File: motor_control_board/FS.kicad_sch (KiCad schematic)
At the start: 18 parts

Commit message: Minor schematic edits
Annotated schematic, selected mosfet and diodes, addressed comments
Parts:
- removed C?: 100n, symbol canhw:C
- removed JP?: Jumper, symbol canhw:SolderJumper_2_Open
- removed R?: 10k, symbol canhw:R_US
- C? (x2): value 15p -> 26p
- X?: value 16MHz -> 12MHz
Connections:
- net MCLR_FS: now also C?.1
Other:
- note added: "DNM when programming"
- note added: "Debug LEDs"
- note added: "Series resistor if necessary"
- moved on the sheet: C?

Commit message: Added second encoder connection, minor edits
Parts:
- added R14, R17: 10k, symbol Device:R_US
- C7: renamed from C?; value 100n -> 10u
- gave numbers to parts that had none: 14
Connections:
- net +5V: now also R14.1
- net FS_MCU: now also R17.1
- net GND: now also R17.2
- net MCLR_FS: now also R14.2
- net ENC2: now reaches U5.18 (RC7)
- net ENC renamed ENC1
- no-connect marks 9 -> 8
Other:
- note added: "DNP until flight"
- note removed: "DNM when programming"

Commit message: assigned footprints
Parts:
- C10, C11, C7, C8, C9: footprint (none) -> Capacitor_SMD:C_0805_2012Metric_Pad1.18x1.45mm_HandSolder
- D7, D8: footprint (none) -> LED_SMD:LED_1206_3216Metric_Pad1.42x1.75mm_HandSolder
- R11, R12, R13, R14, R15, R16, R17: footprint (none) -> Resistor_SMD:R_0805_2012Metric_Pad1.20x1.40mm_HandSolder
- U4: footprint (none) -> Package_SO:SOIC-8_3.9x4.9mm_P1.27mm
- U5: footprint (none) -> Package_SO:SSOP-28_5.3x10.2mm_P0.65mm
- X2: footprint Crystal:Crystal_SMD_2016-4Pin_2.0x1.6mm -> Crystal:Crystal_SMD_Abracon_ABM8G-4Pin_3.2x2.5mm
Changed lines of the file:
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@@
 			)
 		)
-		(property "Footprint" ""
+		(property "Footprint" "Resistor_SMD:R_0805_2012Metric_Pad1.20x1.40mm_HandSolder"
 			(at 136.906 68.834 90)
 			(effects
@@
 			)
 		)
-		(property "Footprint" ""
+		(property "Footprint" "Resistor_SMD:R_0805_2012Metric_Pad1.20x1.40mm_HandSolder"
 			(at 251.206 92.329 90)
 			(effects
@@
 			)
 		)
-		(property "Footprint" ""
+		(property "Footprint" "Package_SO:SOIC-8_3.9x4.9mm_P1.27mm"
 			(at 85.09 151.765 0)
 			(effects
@@
 			)
 		)
-		(property "Footprint" ""
+		(property "Footprint" "Capacitor_SMD:C_0805_2012Metric_Pad1.18x1.45mm_HandSolder"
 			(at 55.5752 149.86 0)
 			(effects
@@
 			)
 		)
-		(property "Footprint" ""
+		(property "Footprint" "Resistor_SMD:R_0805_2012Metric_Pad1.20x1.40mm_HandSolder"
 			(at 175.006 78.486 90)
 			(effects
@@
 			)
 		)
-		(property "Footprint" "Crystal:Crystal_SMD_2016-4Pin_2.0x1.6mm"
+		(property "Footprint" "Crystal:Crystal_SMD_Abracon_ABM8G-4Pin_3.2x2.5mm"
 			(at 72.39 71.12 0)
 			(effects
@@
 			)
 		)
-		(property "Footprint" ""
+		(property "Footprint" "Resistor_SMD:R_0805_2012Metric_Pad1.20x1.40mm_HandSolder"
 			(at 147.066 68.834 90)
 			(effects
@@
 			)
 		)
-		(property "Footprint" ""
+		(property "Footprint" "Resistor_SMD:R_0805_2012Metric_Pad1.20x1.40mm_HandSolder"
 			(at 161.036 71.374 90)
 			(effects
@@
 			)
 		)
-		(property "Footprint" ""
+		(property "Footprint" "Resistor_SMD:R_0805_2012Metric_Pad1.20x1.40mm_HandSolder"
 			(at 243.586 86.106 90)
 			(effects
@@
 			)
 		)
-		(property "Footprint" ""
+		(property "Footprint" "Resistor_SMD:R_0805_2012Metric_Pad1.20x1.40mm_HandSolder"
 			(at 53.594 70.104 90)
 			(effects
@@
 			)
 		)
-		(property "Footprint" ""
+		(property "Footprint" "Capacitor_SMD:C_0805_2012Metric_Pad1.18x1.45mm_HandSolder"
 			(at 160.9852 93.98 0)
 			(effects
@@
 			)
 		)
-		(property "Footprint" ""
+		(property "Footprint" "LED_SMD:LED_1206_3216Metric_Pad1.42x1.75mm_HandSolder"
 			(at 146.05 57.15 0)
 			(effects
@@
 			)
 		)
-		(property "Footprint" ""
+		(property "Footprint" "Capacitor_SMD:C_0805_2012Metric_Pad1.18x1.45mm_HandSolder"
 			(at 61.9252 83.82 0)
 			(effects
@@
 			)
 		)
-		(property "Footprint" ""
+		(property "Footprint" "Package_SO:SSOP-28_5.3x10.2mm_P0.65mm"
 			(at 213.36 93.98 0)
 			(effects
@@
 			)
 		)
-		(property "Footprint" ""
+		(property "Footprint" "Capacitor_SMD:C_0805_2012Metric_Pad1.18x1.45mm_HandSolder"
 			(at 84.7852 83.82 0)
 			(effects
@@
 			)
 		)
-		(property "Footprint" ""
+		(property "Footprint" "LED_SMD:LED_1206_3216Metric_Pad1.42x1.75mm_HandSolder"
 			(at 135.89 57.15 0)
 			(effects
@@
 			)
 		)
-		(property "Footprint" ""
+		(property "Footprint" "Capacitor_SMD:C_0805_2012Metric_Pad1.18x1.45mm_HandSolder"
 			(at 237.1852 77.47 0)
 			(effects

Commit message: PCB routing 70% done
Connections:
- net ENC1: now also U5.4 (RA2); no longer U5.21 (RB0)
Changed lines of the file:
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@@
+	)
+	(no_connect
+		(at 219.71 97.79)
+	)
+	(no_connect
+		(at 219.71 102.87)
+	)
+	(no_connect
+		(at 182.88 90.17)
+	)
+	(no_connect
+		(at 219.71 105.41)
 	)
 	(no_connect
 		(at 182.88 92.71)
-	)
-	(no_connect
-		(at 182.88 85.09)
-	)
-	(no_connect
-		(at 219.71 102.87)
-	)
-	(no_connect
-		(at 182.88 90.17)
-	)
-	(no_connect
-		(at 219.71 105.41)
 	)
 	(wire
@@
 	(hierarchical_label "ENC1"
 		(shape input)
-		(at 219.71 97.79 0)
-		(fields_autoplaced yes)
-		(effects
-			(font
-				(size 1.27 1.27)
-			)
-			(justify left)
-		)
-	)
+		(at 182.88 85.09 180)
+		(fields_autoplaced yes)
+		(effects
+			(font
+				(size 1.27 1.27)
+			)
+			(justify right)
+		)
+	)

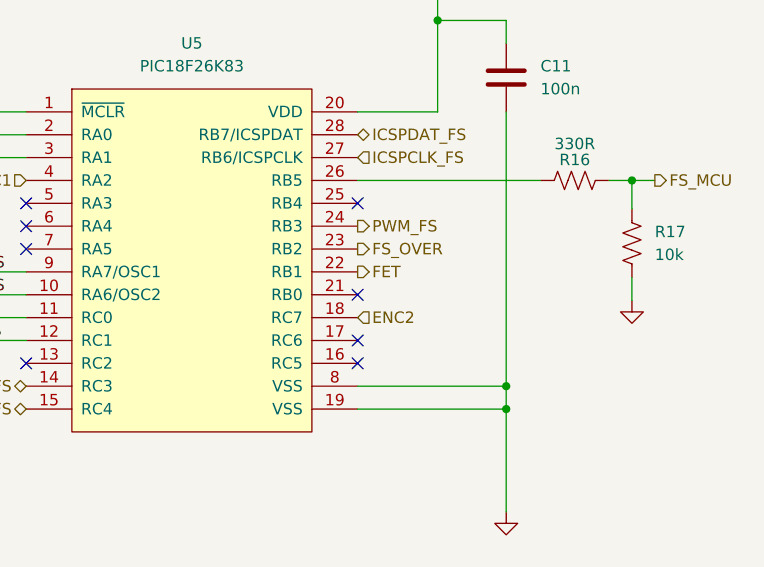
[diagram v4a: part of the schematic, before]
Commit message: Routing Complete
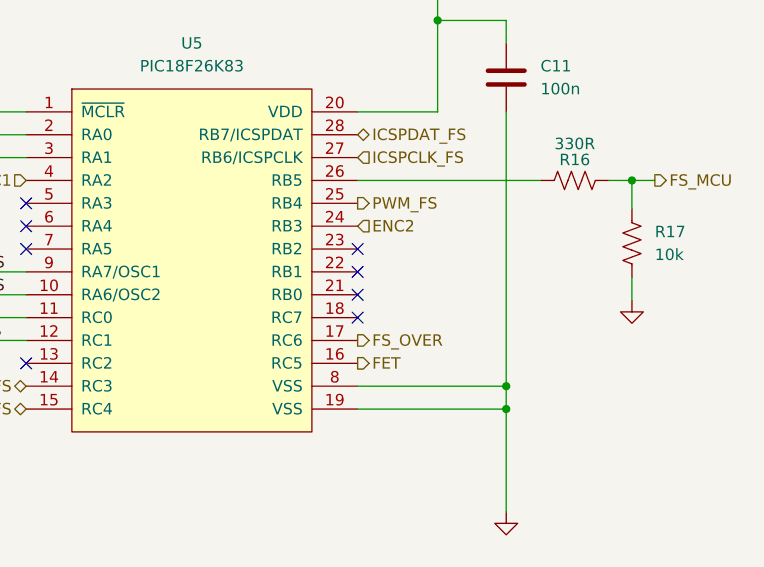
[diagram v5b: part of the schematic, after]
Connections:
- net ENC2: now also U5.24 (RB3); no longer U5.18 (RC7)
- net FET: now also U5.16 (RC5); no longer U5.22 (RB1)
- net FS_OVER: now also U5.17 (RC6); no longer U5.23 (RB2)
- net PWM_FS: now also U5.25 (RB4); no longer U5.24 (RB3)
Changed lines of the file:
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@@
 	)
 	(no_connect
-		(at 219.71 87.63)
+		(at 219.71 95.25)
 	)
 	(no_connect
@@
 	)
 	(no_connect
+		(at 219.71 100.33)
+	)
+	(no_connect
 		(at 219.71 97.79)
 	)
 	(no_connect
-		(at 219.71 102.87)
+		(at 219.71 92.71)
 	)
 	(no_connect
 		(at 182.88 90.17)
-	)
-	(no_connect
-		(at 219.71 105.41)
 	)
 	(no_connect
@@
 	(hierarchical_label "ENC2"
 		(shape input)
-		(at 219.71 100.33 0)
+		(at 219.71 90.17 0)
 		(fields_autoplaced yes)
 		(effects
@@
 	(hierarchical_label "FS_OVER"
 		(shape output)
-		(at 219.71 92.71 0)
+		(at 219.71 102.87 0)
 		(fields_autoplaced yes)
 		(effects
@@
 	(hierarchical_label "FET"
 		(shape output)
-		(at 219.71 95.25 0)
+		(at 219.71 105.41 0)
 		(fields_autoplaced yes)
 		(effects
@@
 	(hierarchical_label "PWM_FS"
 		(shape output)
-		(at 219.71 90.17 0)
-		(fields_autoplaced yes)
-		(effects
+		(at 219.71 87.63 0)
+		(fields_autoplaced yes)
+		(effects

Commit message: Fixed symbol and footprint libraries
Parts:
- R14, R17: symbol Device:R_US -> canhw:R_US
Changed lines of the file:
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@@
 	)
 	(symbol
-		(lib_id "Device:R_US")
+		(lib_id "canhw:R_US")
 		(at 250.19 92.075 0)
 		(unit 1)
@@
 	)
 	(symbol
-		(lib_id "Device:R_US")
+		(lib_id "canhw:R_US")
 		(at 160.02 71.12 0)
 		(unit 1)
